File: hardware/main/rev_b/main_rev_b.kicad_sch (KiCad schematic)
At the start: 0 parts

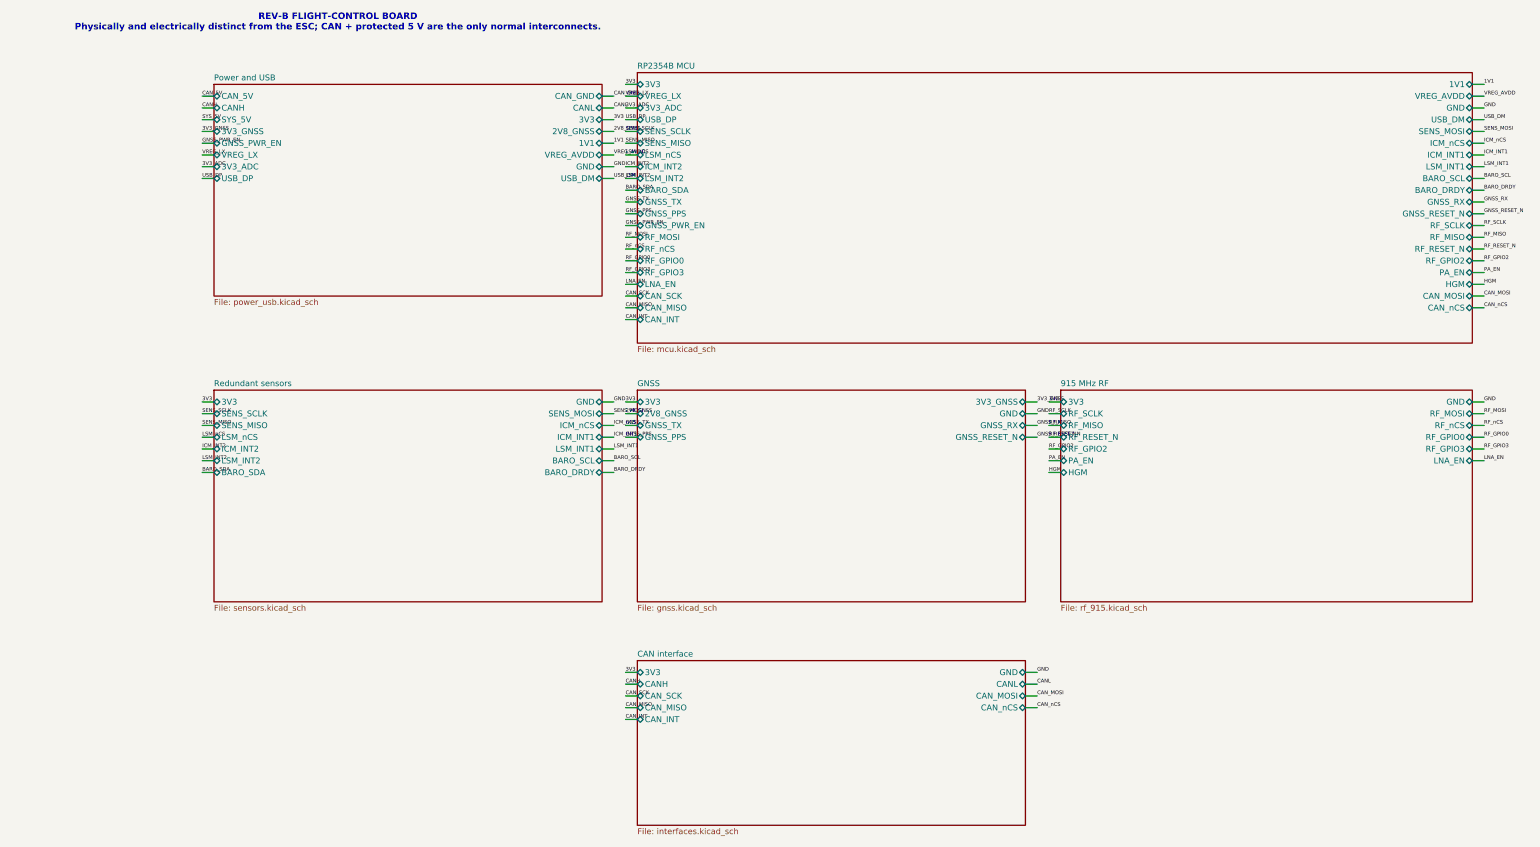
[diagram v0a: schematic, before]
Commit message: Add Main Rev B ESC interfaces
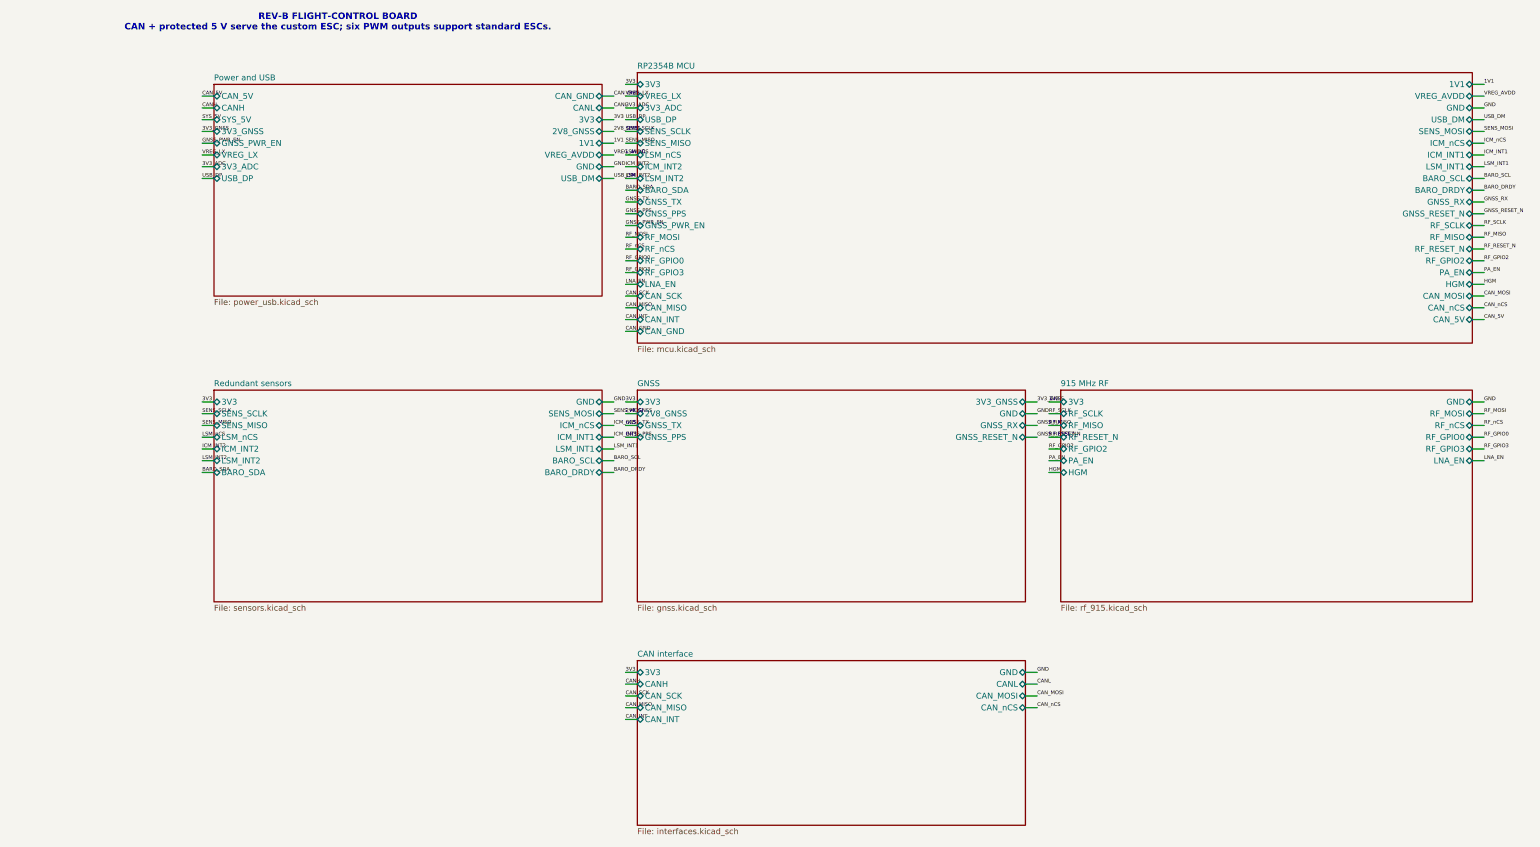
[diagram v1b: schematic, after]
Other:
- sheet RP2354B MCU ports: added CAN_5V, CAN_GND; removed none
- note added: "REV-B FLIGHT-CONTROL BOARD CAN + protected 5 V serve the custom ESC; six PWM outputs support standard ESCs."
- note removed: "REV-B FLIGHT-CONTROL BOARD Physically and electrically distinct from the ESC; CAN + protected 5 V are the only normal interconnects."
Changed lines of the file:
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@@
+		)
+	)
+	(wire
+		(pts
+			(xy 287.02 76.2) (xy 289.56 76.2)
+		)
+		(stroke
+			(width 0)
+			(type default)
+		)
+	)
+	(wire
+		(pts
+			(xy 106.68 78.74) (xy 104.14 78.74)
+		)
+		(stroke
+			(width 0)
+			(type default)
 		)
 	)
@@
 		)
 	)
-	(text "REV-B FLIGHT-CONTROL BOARD\nPhysically and electrically distinct from the ESC; CAN + protected 5 V are the only normal interconnects."
+	(label "CAN_5V"
+		(at 289.56 76.2 0)
+		(effects
+			(font
+				(size 0.8 0.8)
+			)
+			(justify left bottom)
+		)
+	)
+	(label "CAN_GND"
+		(at 104.14 78.74 0)
+		(effects
+			(font
+				(size 0.8 0.8)
+			)
+			(justify left bottom)
+		)
+	)
+	(text "REV-B FLIGHT-CONTROL BOARD\nCAN + protected 5 V serve the custom ESC; six PWM outputs support standard ESCs."
 		(exclude_from_sim no)
 		(at 42 12 0.0000)
@@
 			)
 		)
+		(pin "CAN_5V" bidirectional
+			(at 287.02 76.2 0)
+			(effects
+				(font
+					(size 1.27 1.27)
+				)
+				(justify right)
+			)
+		)
+		(pin "CAN_GND" bidirectional
+			(at 106.68 78.74 180)
+			(effects
+				(font
+					(size 1.27 1.27)
+				)
+				(justify left)
+			)
+		)
